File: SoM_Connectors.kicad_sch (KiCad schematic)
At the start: 5 parts, among them SW1 SW_DIP_x02

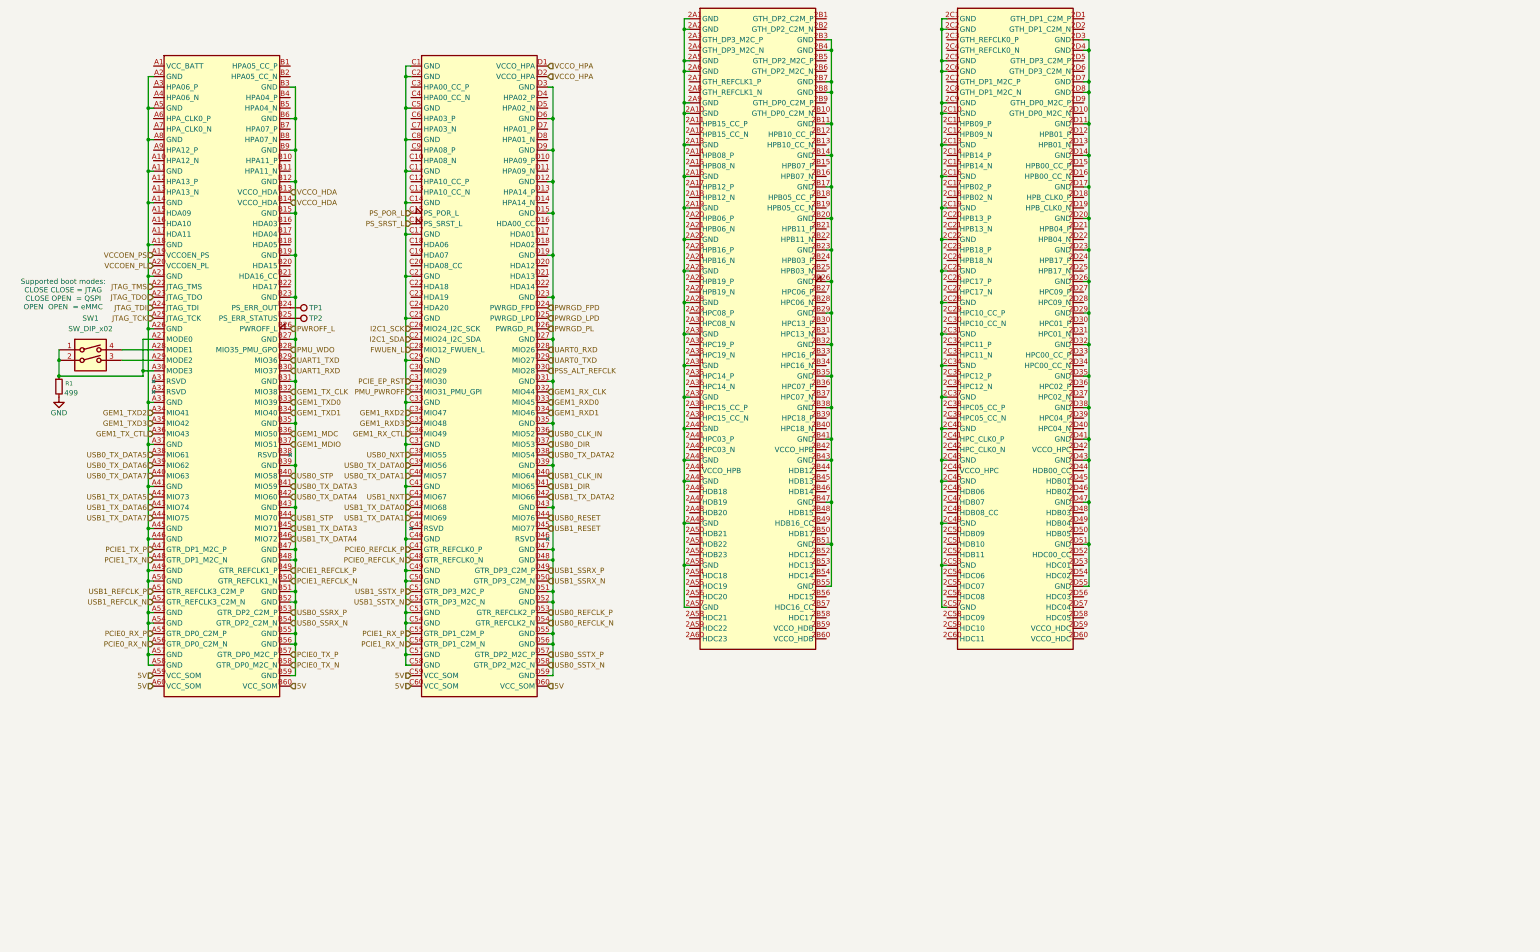
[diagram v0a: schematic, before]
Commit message: converted JTAG, GEM1, PCIE, and USB to busses
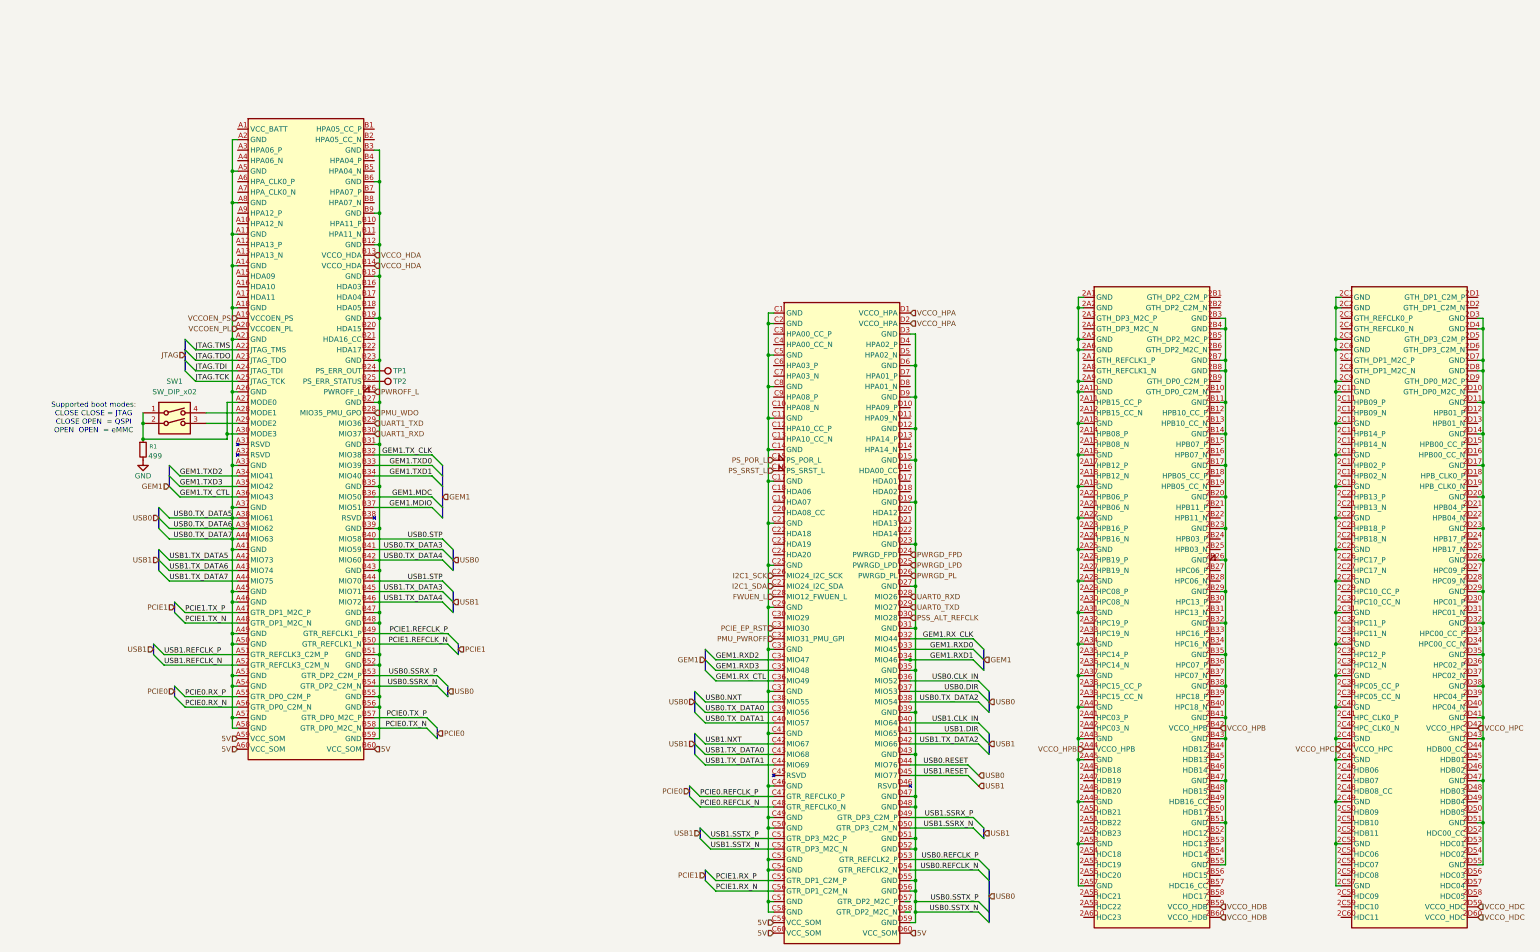
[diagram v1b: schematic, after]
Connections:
- net USB0_TX_DATA5 is gone; now on net USB0.TX_DATA5: U1.A38 (MIO61)
- net USB0_TX_DATA6 is gone; now on net USB0.TX_DATA5: U1.A39 (MIO62)
- net USB0_TX_DATA7 is gone; now on net USB0.TX_DATA5: U1.A40 (MIO63)
- net USB0.TX_DATA5: now reaches U1.A11 (GND), U1.A14 (GND), U1.A18 (GND), U1.A2 (GND), U1.A21 (GND), U1.A26 (GND), U1.A33 (GND), U1.A37 (GND), U1.A41 (GND), U1.A45 (GND), U1.A46 (GND), U1.A49 (GND), U1.A5 (GND), U1.A50 (GND), U1.A53 (GND), U1.A54 (GND), U1.A57 (GND), U1.A58 (GND), U1.A8 (GND)
- net USB0.SSTX_N: now reaches U1.D12 (GND), U1.D15 (GND), U1.D19 (GND), U1.D23 (GND), U1.D27 (GND), U1.D3 (GND), U1.D31 (GND), U1.D35 (GND), U1.D39 (GND), U1.D43 (GND), U1.D47 (GND), U1.D48 (GND), U1.D51 (GND), U1.D52 (GND), U1.D55 (GND), U1.D56 (GND), U1.D59 (GND), U1.D6 (GND), U1.D9 (GND)
- net VCCO_HPB: now reaches U1.2A44 (VCCO_HPB)
- net VCCO_HPB: now also U1.2B42 (VCCO_HPB)
- net VCCO_HDB: now reaches U1.2B59 (VCCO_HDB)
- net VCCO_HDB: now also U1.2B60 (VCCO_HDB)
- net VCCO_HPC: now reaches U1.2C44 (VCCO_HPC)
- net VCCO_HPC: now also U1.2D42 (VCCO_HPC)
- net VCCO_HDC: now reaches U1.2D59 (VCCO_HDC)
- net VCCO_HDC: now also U1.2D60 (VCCO_HDC)
- net GEM1_MDC renamed GEM1.MDC
- net GEM1_MDIO renamed GEM1.MDIO
- net GEM1_RXD0 renamed GEM1.RXD0
- net GEM1_RXD1 renamed GEM1.RXD1
- net GEM1_RXD2 renamed GEM1.RXD2
- net GEM1_RXD3 renamed GEM1.RXD3
- net GEM1_RX_CLK renamed GEM1.RX_CLK
- net GEM1_RX_CTL renamed GEM1.RX_CTL
- net GEM1_TXD0 renamed GEM1.TXD0
- net GEM1_TXD1 renamed GEM1.TXD1
- net GEM1_TXD2 renamed GEM1.TXD2
- net GEM1_TXD3 renamed GEM1.TXD3
- net GEM1_TX_CLK renamed GEM1.TX_CLK
- net GEM1_TX_CTL renamed GEM1.TX_CTL
- net JTAG_TCK renamed JTAG.TCK
- net JTAG_TDI renamed JTAG.TDI
- net JTAG_TDO renamed JTAG.TDO
- net JTAG_TMS renamed JTAG.TMS
- net PCIE0_REFCLK_N renamed PCIE0.REFCLK_N
- net PCIE0_REFCLK_P renamed PCIE0.REFCLK_P
- net PCIE0_RX_N renamed PCIE0.RX_N
- net PCIE0_RX_P renamed PCIE0.RX_P
- net PCIE0_TX_N renamed PCIE0.TX_N
- net PCIE0_TX_P renamed PCIE0.TX_P
- net PCIE1_REFCLK_N renamed PCIE1.REFCLK_N
- net PCIE1_REFCLK_P renamed PCIE1.REFCLK_P
- net PCIE1_RX_N renamed PCIE1.RX_N
- net PCIE1_RX_P renamed PCIE1.RX_P
- net PCIE1_TX_N renamed PCIE1.TX_N
- net PCIE1_TX_P renamed PCIE1.TX_P
- net USB0_CLK_IN renamed USB0.CLK_IN
- net USB0_DIR renamed USB0.DIR
- net USB0_NXT renamed USB0.NXT
- net USB0_REFCLK_N renamed USB0.REFCLK_N
- net USB0_REFCLK_P renamed USB0.REFCLK_P
- net USB0_RESET renamed USB0.RESET
- net USB0_SSRX_N renamed USB0.SSRX_N
- net USB0_SSRX_P renamed USB0.SSRX_P
- net USB0_SSTX_N: no longer names the net of U1.D58 (GTR_DP2_M2C_N)
- net USB0_SSTX_P: no longer names the net of U1.D57 (GTR_DP2_M2C_P)
- net USB0_STP renamed USB0.STP
- net USB0_TX_DATA0 renamed USB0.TX_DATA0
- net USB0_TX_DATA1 renamed USB0.TX_DATA1
- net USB0_TX_DATA2 renamed USB0.TX_DATA2
- net USB0_TX_DATA3 renamed USB0.TX_DATA3
- net USB0_TX_DATA4 renamed USB0.TX_DATA4
- net USB1_CLK_IN renamed USB1.CLK_IN
- net USB1_DIR renamed USB1.DIR
- net USB1_NXT renamed USB1.NXT
- net USB1_REFCLK_N renamed USB1.REFCLK_N
- net USB1_REFCLK_P renamed USB1.REFCLK_P
- net USB1_RESET renamed USB1.RESET
- net USB1_SSRX_N renamed USB1.SSRX_N
- net USB1_SSRX_P renamed USB1.SSRX_P
- net USB1_SSTX_N renamed USB1.SSTX_N
- net USB1_SSTX_P renamed USB1.SSTX_P
- net USB1_STP renamed USB1.STP
- net USB1_TX_DATA0 renamed USB1.TX_DATA0
- net USB1_TX_DATA1 renamed USB1.TX_DATA1
- net USB1_TX_DATA2 renamed USB1.TX_DATA2
- net USB1_TX_DATA3 renamed USB1.TX_DATA3
- net USB1_TX_DATA4 renamed USB1.TX_DATA4
- net USB1_TX_DATA5 renamed USB1.TX_DATA5
- net USB1_TX_DATA6 renamed USB1.TX_DATA6
- net USB1_TX_DATA7 renamed USB1.TX_DATA7
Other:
- moved on the sheet: R1, SW1, TP1, TP2

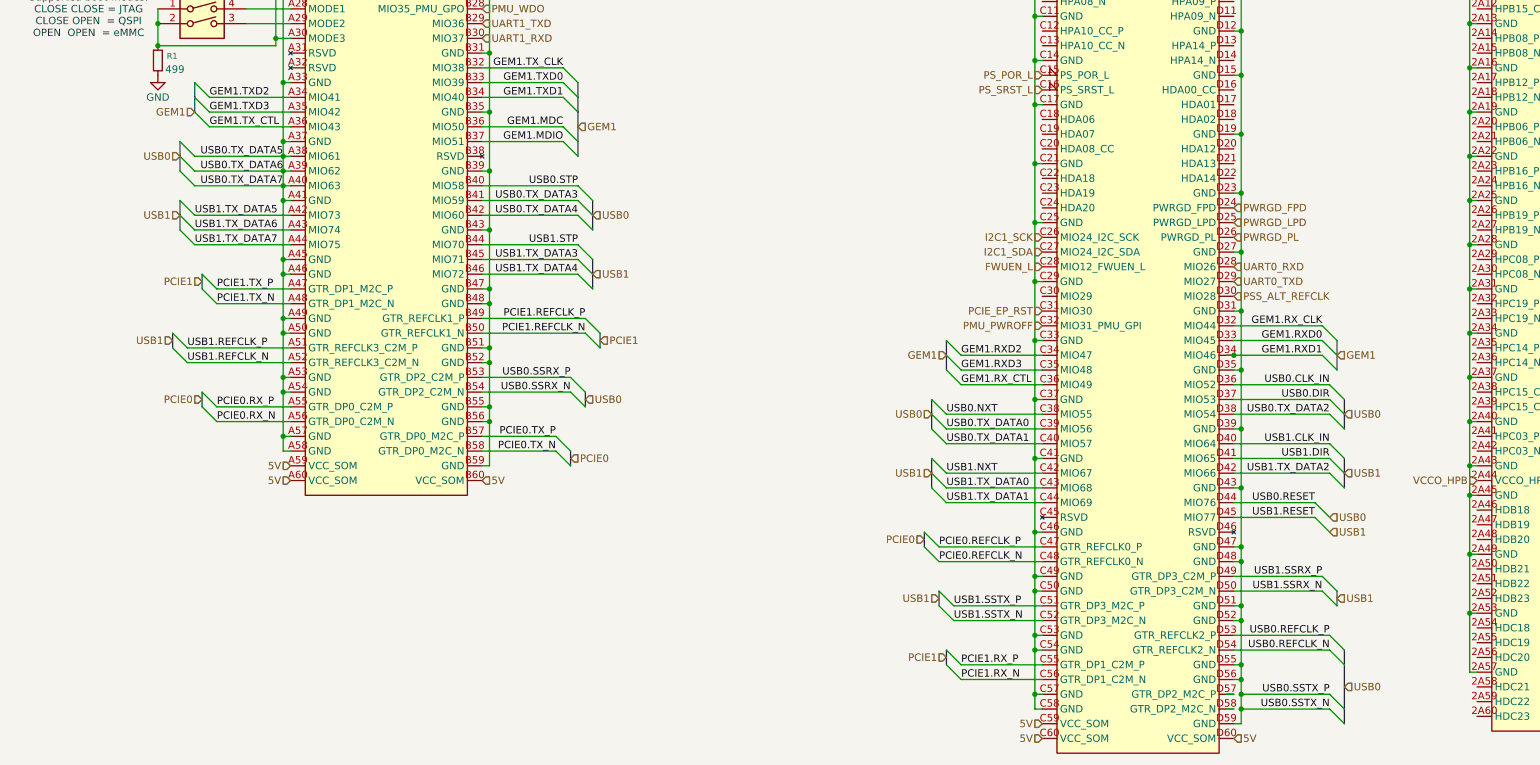
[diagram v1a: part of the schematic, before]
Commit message: preliminary USB-PD subcircuit bus labeling fixes
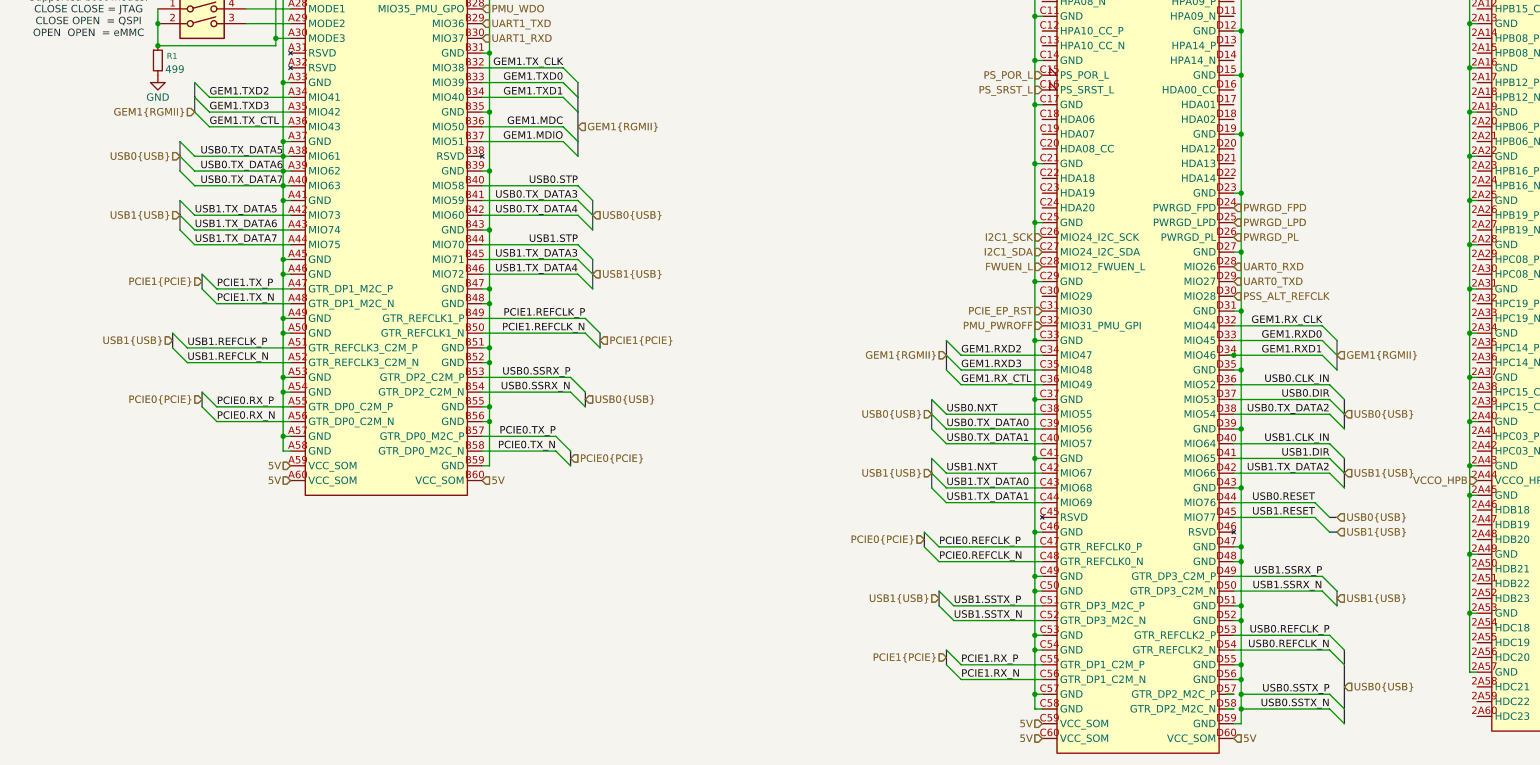
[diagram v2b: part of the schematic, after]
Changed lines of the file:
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@@
 	(generator_version "9.0")
 	(paper "A3")
-	(bus_alias "GEM1"
-		(members "MDC" "MDIO" "TX_CLK" "TXD[0..3]" "TX_CTL" "RX_CLK" "RXD[0..3]"
-			"RX_CTL"
-		)
-	)
 	(bus_alias "JTAG"
 		(members "TMS" "TDO" "TDI" "TCK")
 	)
-	(bus_alias "PCIE0"
+	(bus_alias "PCIE"
 		(members "REFCLK_P" "REFCLK_N" "RX_P" "RX_N" "TX_P" "TX_N")
 	)
-	(bus_alias "PCIE1"
-		(members "REFCLK_P" "REFCLK_N" "RX_P" "RX_N" "TX_P" "TX_N")
-	)
-	(bus_alias "USB0"
-		(members "RST" "CLK_IN" "DIR" "NXT" "STP" "TX_DATA[0..7]" "REFCLK_P" "REFCLK_N"
-			"SSRX_P" "SSRX_N" "SSTX_P" "SSTX_N" "RESET"
+	(bus_alias "RGMII"
+		(members "MDC" "MDIO" "TX_CLK" "TXD[0..3]" "TX_CTL" "RX_CLK" "RXD[0..3]"
+			"RX_CTL"
 		)
 	)
-	(bus_alias "USB1"
+	(bus_alias "USB"
 		(members "RST" "CLK_IN" "DIR" "NXT" "STP" "TX_DATA[0..7]" "REFCLK_P" "REFCLK_N"
 			"SSRX_P" "SSRX_N" "SSTX_P" "SSTX_N" "RESET"
@@
 		)
 	)
+	(bus
+		(pts
+			(xy 238.76 199.39) (xy 240.03 199.39)
+		)
+		(stroke
+			(width 0)
+			(type default)
+		)
+	)
 	(wire
 		(pts
@@
 		)
 	)
+	(bus
+		(pts
+			(xy 238.76 196.85) (xy 240.03 196.85)
+		)
+		(stroke
+			(width 0)
+			(type default)
+		)
+	)
 	(wire
 		(pts
@@
 		)
 	)
-	(hierarchical_label "PCIE1"
+	(hierarchical_label "PCIE1{PCIE}"
 		(shape input)
 		(at 44.45 156.21 180)
@@
 		)
 	)
-	(hierarchical_label "USB0"
+	(hierarchical_label "USB0{USB}"
 		(shape input)
 		(at 241.3 226.06 0)
@@
 		)
 	)
-	(hierarchical_label "USB0"
+	(hierarchical_label "USB0{USB}"
 		(shape input)
 		(at 241.3 179.07 0)
@@
 		)
 	)
-	(hierarchical_label "USB0"
+	(hierarchical_label "USB0{USB}"
 		(shape input)
-		(at 238.76 196.85 0)
+		(at 240.03 196.85 0)
 		(effects
 			(font
@@
 		)
 	)
-	(hierarchical_label "USB1"
+	(hierarchical_label "USB1{USB}"
 		(shape input)
 		(at 170.18 189.23 180)
@@
 		)
 	)
-	(hierarchical_label "USB1"
+	(hierarchical_label "USB1{USB}"
 		(shape input)
 		(at 39.37 166.37 180)
@@
 		)
 	)
-	(hierarchical_label "PCIE1"
+	(hierarchical_label "PCIE1{PCIE}"
 		(shape input)
 		(at 172.72 220.98 180)
@@
 		)
 	)
-	(hierarchical_label "GEM1"
+	(hierarchical_label "GEM1{RGMII}"
 		(shape input)
 		(at 109.22 129.54 0)
@@
 		)
 	)
-	(hierarchical_label "USB1"
+	(hierarchical_label "USB1{USB}"
 		(shape input)
 		(at 171.45 210.82 180)
@@
 		)
 	)
-	(hierarchical_label "USB0"
+	(hierarchical_label "USB0{USB}"
 		(shape input)
 		(at 170.18 179.07 180)
@@
 		)
 	)
-	(hierarchical_label "GEM1"
+	(hierarchical_label "GEM1{RGMII}"
 		(shape input)
 		(at 43.18 127 180)
@@
 		)
 	)
-	(hierarchical_label "PCIE0"
+	(hierarchical_label "PCIE0{PCIE}"
 		(shape input)
 		(at 44.45 176.53 180)
@@
 		)
 	)
-	(hierarchical_label "GEM1"
+	(hierarchical_label "GEM1{RGMII}"
 		(shape input)
 		(at 172.72 168.91 180)
@@
 		)
 	)
-	(hierarchical_label "PCIE1"
+	(hierarchical_label "PCIE1{PCIE}"
 		(shape input)
 		(at 113.03 166.37 0)
@@
 		)
 	)
-	(hierarchical_label "USB0"
+	(hierarchical_label "USB0{USB}"
 		(shape input)
 		(at 110.49 176.53 0)
@@
 		)
 	)
-	(hierarchical_label "PCIE0"
+	(hierarchical_label "PCIE0{PCIE}"
 		(shape input)
 		(at 168.91 200.66 180)
@@
 		)
 	)
-	(hierarchical_label "USB0"
+	(hierarchical_label "USB0{USB}"
 		(shape input)
 		(at 111.76 144.78 0)
@@
 		)
 	)
-	(hierarchical_label "PCIE0"
+	(hierarchical_label "PCIE0{PCIE}"
 		(shape input)
 		(at 107.95 186.69 0)
@@
 		)
 	)
-	(hierarchical_label "USB1"
+	(hierarchical_label "USB1{USB}"
 		(shape input)
 		(at 240.03 210.82 0)
@@
 		)
 	)
-	(hierarchical_label "USB1"
+	(hierarchical_label "USB1{USB}"
 		(shape input)
 		(at 40.64 144.78 180)
@@
 		)
 	)
-	(hierarchical_label "USB1"
+	(hierarchical_label "USB1{USB}"
 		(shape input)
 		(at 241.3 189.23 0)
@@
 		)
 	)
-	(hierarchical_label "USB1"
+	(hierarchical_label "USB1{USB}"
 		(shape input)
-		(at 238.76 199.39 0)
+		(at 240.03 199.39 0)
 		(effects
 			(font
@@
 		)
 	)
-	(hierarchical_label "USB1"
+	(hierarchical_label "USB1{USB}"
 		(shape input)
 		(at 111.76 154.94 0)
@@
 		)
 	)
-	(hierarchical_label "GEM1"
+	(hierarchical_label "GEM1{RGMII}"
 		(shape input)
 		(at 240.03 168.91 0)
@@
 		)
 	)
-	(hierarchical_label "USB0"
+	(hierarchical_label "USB0{USB}"
 		(shape input)
 		(at 40.64 134.62 180)
